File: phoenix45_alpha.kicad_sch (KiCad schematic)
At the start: 124 parts, among them J1 AVR-ISP-6, SW1 SW_PUSH, SW2 SW_PUSH, U1 SRV05-4, U3 ATmega32U4-M, X1 Crystal_GND24_Small

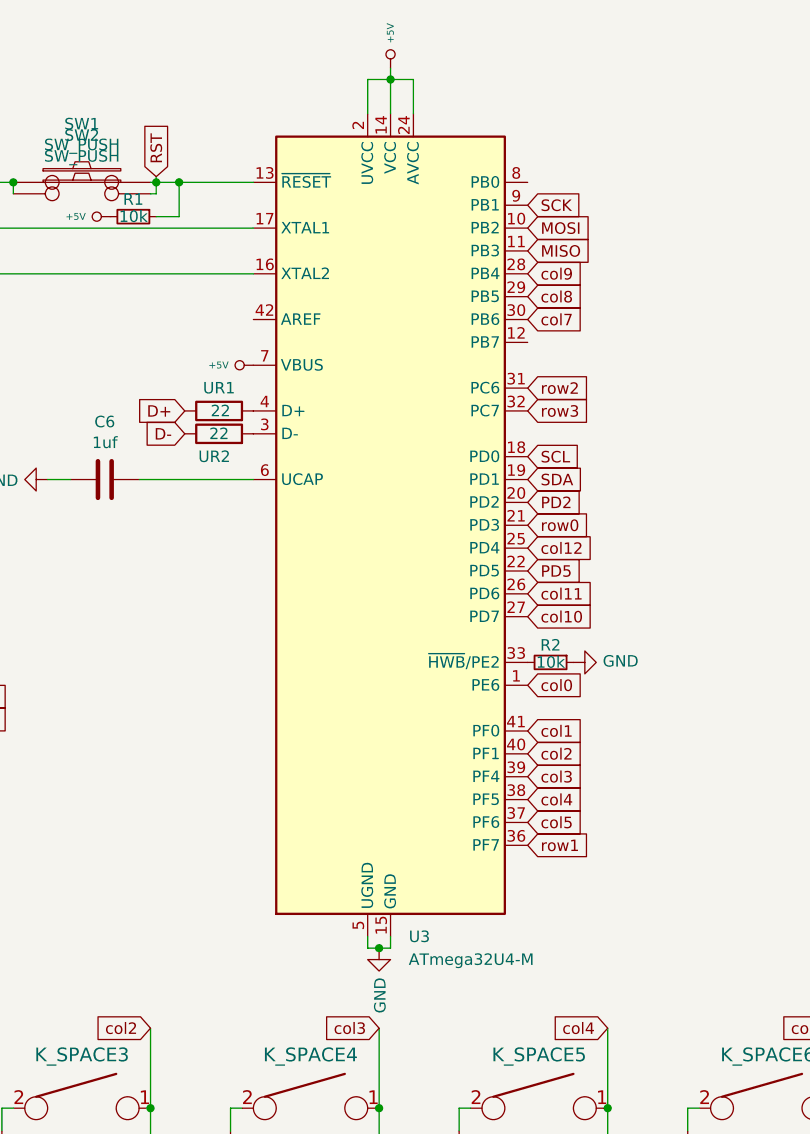
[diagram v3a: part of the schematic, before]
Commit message: qfn + tqfp
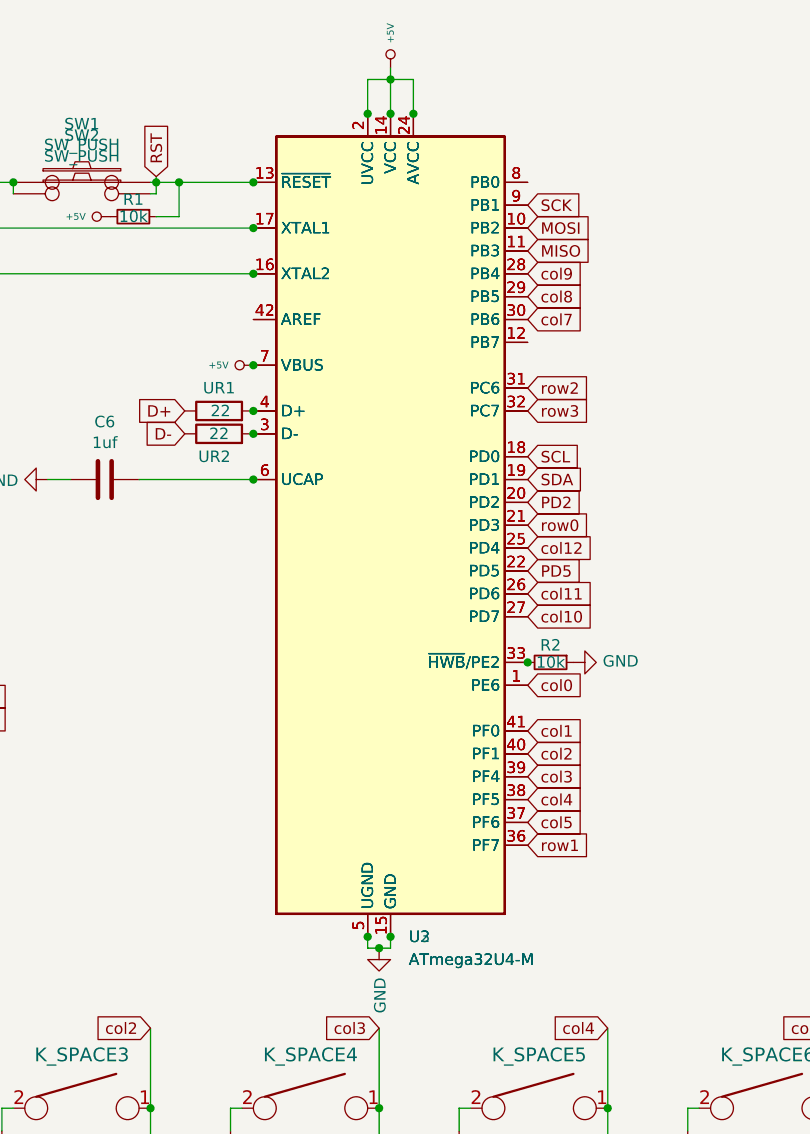
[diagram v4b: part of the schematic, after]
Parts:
- added U2: ATmega32U4-M, Package_DFN_QFN:QFN-44-1EP_7x7mm_P0.5mm_EP5.2x5.2mm_ThermalVias, symbol MCU_Microchip_ATmega:ATmega32U4-M
- U3: footprint Package_DFN_QFN:QFN-44-1EP_7x7mm_P0.5mm_EP5.2x5.2mm_ThermalVias -> Package_QFP:TQFP-44_10x10mm_P0.8mm
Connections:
- net +5V: now also U2.14 (VCC), U2.2 (UVCC), U2.24 (AVCC), U2.34 (VCC), U2.44 (AVCC), U2.7 (VBUS)
- net GND: now also U2.15 (GND), U2.23 (GND), U2.35 (GND), U2.43 (GND), U2.45 (GND), U2.5 (UGND)
- net MISO: now also U2.11 (PB3)
- net MOSI: now also U2.10 (PB2)
- net PD2: now also U2.20 (PD2)
- net PD5: now also U2.22 (PD5)
- net RST: now also U2.13 (~{RESET})
- net SCK: now also U2.9 (PB1)
- net SCL: now also U2.18 (PD0)
- net SDA: now also U2.19 (PD1)
- net col0: now also U2.1 (PE6)
- net col1: now also U2.41 (PF0)
- net col10: now also U2.27 (PD7)
- net col11: now also U2.26 (PD6)
- net col12: now also U2.25 (PD4)
- net col2: now also U2.40 (PF1)
- net col3: now also U2.39 (PF4)
- net col4: now also U2.38 (PF5)
- net col5: now also U2.37 (PF6)
- net col7: now also U2.30 (PB6)
- net col8: now also U2.29 (PB5)
- net col9: now also U2.28 (PB4)
- net row0: now also U2.21 (PD3)
- net row1: now also U2.36 (PF7)
- net row2: now also U2.31 (PC6)
- net row3: now also U2.32 (PC7)
- net at C7.1, U3.17 (XTAL1), X1.1: now also U2.17 (XTAL1)
- net at C8.1, U3.16 (XTAL2), X1.3: now also U2.16 (XTAL2)
- net at U3.4 (D+), UR2.2: now also U2.4 (D+)
- net at U3.3 (D-), UR1.2: now also U2.3 (D-)
- net at C6.1, U3.6 (UCAP): now also U2.6 (UCAP)
- net at R2.2, U3.33 (~{HWB}/PE2): now also U2.33 (~{HWB}/PE2)
- net at U3.12 (PB7): now also U2.12 (PB7)
- net at U3.42 (AREF): now also U2.42 (AREF)
- net at U3.8 (PB0): now also U2.8 (PB0)
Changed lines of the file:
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@@
   (junction (at 149.86 245.11) (diameter 0) (color 0 0 0 0)
   )
+  (junction (at 127 60.96) (diameter 0) (color 0 0 0 0)
+  )
   (junction (at 166.37 184.15) (diameter 0) (color 0 0 0 0)
   )
   (junction (at 233.045 66.675) (diameter 0) (color 0 0 0 0)
   )
+  (junction (at 142.24 48.26) (diameter 0) (color 0 0 0 0)
+  )
   (junction (at 140.97 158.75) (diameter 0) (color 0 0 0 0)
   )
@@
   (junction (at 140.97 140.97) (diameter 0) (color 0 0 0 0)
   )
+  (junction (at 139.7 139.7) (diameter 0) (color 0 0 0 0)
+  )
   (junction (at 251.46 219.71) (diameter 0) (color 0 0 0 0)
   )
   (junction (at 294.64 109.22) (diameter 0) (color 0 0 0 0)
   )
+  (junction (at 127 66.04) (diameter 0) (color 0 0 0 0)
+  )
   (junction (at 175.26 194.31) (diameter 0) (color 0 0 0 0)
   )
@@
   (junction (at 38.735 105.41) (diameter 0) (color 0 0 0 0)
   )
+  (junction (at 127 88.9) (diameter 0) (color 0 0 0 0)
+  )
   (junction (at 31.115 105.41) (diameter 0) (color 0 0 0 0)
   )
@@
   (junction (at 302.26 219.71) (diameter 0) (color 0 0 0 0)
   )
+  (junction (at 127 55.88) (diameter 0) (color 0 0 0 0)
+  )
   (junction (at 48.26 194.31) (diameter 0) (color 0 0 0 0)
   )
@@
   (junction (at 276.86 194.31) (diameter 0) (color 0 0 0 0)
   )
+  (junction (at 127 76.2) (diameter 0) (color 0 0 0 0)
+  )
   (junction (at 318.77 209.55) (diameter 0) (color 0 0 0 0)
   )
@@
   (junction (at 73.66 194.31) (diameter 0) (color 0 0 0 0)
   )
+  (junction (at 142.24 139.7) (diameter 0) (color 0 0 0 0)
+  )
   (junction (at 251.46 194.31) (diameter 0) (color 0 0 0 0)
   )
   (junction (at 318.77 158.75) (diameter 0) (color 0 0 0 0)
   )
+  (junction (at 139.7 48.26) (diameter 0) (color 0 0 0 0)
+  )
+  (junction (at 127 83.82) (diameter 0) (color 0 0 0 0)
+  )
   (junction (at 293.37 158.75) (diameter 0) (color 0 0 0 0)
   )
@@
   (junction (at 115.57 184.15) (diameter 0) (color 0 0 0 0)
   )
+  (junction (at 144.78 48.26) (diameter 0) (color 0 0 0 0)
+  )
   (junction (at 318.77 184.15) (diameter 0) (color 0 0 0 0)
   )
@@
   (junction (at 267.97 158.75) (diameter 0) (color 0 0 0 0)
   )
+  (junction (at 127 81.28) (diameter 0) (color 0 0 0 0)
+  )
   (junction (at 72.39 77.47) (diameter 0) (color 0 0 0 0)
   )
@@
   (junction (at 344.17 158.75) (diameter 0) (color 0 0 0 0)
   )
+  (junction (at 157.48 109.22) (diameter 0) (color 0 0 0 0)
+  )
   (junction (at 166.37 209.55) (diameter 0) (color 0 0 0 0)
   )
@@
     (pin "2")
   )
+  (symbol (lib_id "MCU_Microchip_ATmega:ATmega32U4-M") (at 142.24 93.98 0) (unit 1)
+    (in_bom yes) (on_board yes) (fields_autoplaced)
+    (property "Reference" "U2" (id 0) (at 144.2594 139.7 0)
+      (effects (font (size 1.27 1.27)) (justify left))
+    )
+    (property "Value" "ATmega32U4-M" (id 1) (at 144.2594 142.24 0)
+      (effects (font (size 1.27 1.27)) (justify left))
+    )
+    (property "Footprint" "Package_DFN_QFN:QFN-44-1EP_7x7mm_P0.5mm_EP5.2x5.2mm_ThermalVias" (id 2) (at 142.24 93.98 0)
+      (effects (font (size 1.27 1.27) italic) hide)
+    )
+    (property "Datasheet" "http://ww1.microchip.com/downloads/en/DeviceDoc/Atmel-7766-8-bit-AVR-ATmega16U4-32U4_Datasheet.pdf" (id 3) (at 142.24 93.98 0)
+      (effects (font (size 1.27 1.27)) hide)
+    )
+    (pin "1")
+    (pin "10")
+    (pin "11")
+    (pin "12")
+    (pin "13")
+    (pin "14")
+    (pin "15")
+    (pin "16")
+    (pin "17")
+    (pin "18")
+    (pin "19")
+    (pin "2")
+    (pin "20")
+    (pin "21")
+    (pin "22")
+    (pin "23")
+    (pin "24")
+    (pin "25")
+    (pin "26")
+    (pin "27")
+    (pin "28")
+    (pin "29")
+    (pin "3")
+    (pin "30")
+    (pin "31")
+    (pin "32")
+    (pin "33")
+    (pin "34")
+    (pin "35")
+    (pin "36")
+    (pin "37")
+    (pin "38")
+    (pin "39")
+    (pin "4")
+    (pin "40")
+    (pin "41")
+    (pin "42")
+    (pin "43")
+    (pin "44")
+    (pin "45")
+    (pin "5")
+    (pin "6")
+    (pin "7")
+    (pin "8")
+    (pin "9")
+  )
   (symbol (lib_id "keyboard_parts:SW_PUSH") (at 107.95 57.15 0) (unit 1)
     (in_bom yes) (on_board yes)
@@
   )
   (symbol (lib_id "MCU_Microchip_ATmega:ATmega32U4-M") (at 142.24 93.98 0) (unit 1)
-    (in_bom yes) (on_board yes) (fields_autoplaced)
+    (in_bom yes) (on_board yes)
     (property "Reference" "U3" (id 0) (at 144.2594 139.7 0)
       (effects (font (size 1.27 1.27)) (justify left))
@@
       (effects (font (size 1.27 1.27)) (justify left))
     )
-    (property "Footprint" "Package_DFN_QFN:QFN-44-1EP_7x7mm_P0.5mm_EP5.2x5.2mm_ThermalVias" (id 2) (at 142.24 93.98 0)
+    (property "Footprint" "Package_QFP:TQFP-44_10x10mm_P0.8mm" (id 2) (at 142.24 93.98 0)
       (effects (font (size 1.27 1.27) italic) hide)
     )
@@
       (reference "U1") (unit 1) (value "SRV05-4") (footprint "Package_TO_SOT_SMD:SOT-23-6_Handsoldering")
     )
+    (path "/1ced1425-3090-4db4-a173-4dd40d7cc299"
+      (reference "U2") (unit 1) (value "ATmega32U4-M") (footprint "Package_DFN_QFN:QFN-44-1EP_7x7mm_P0.5mm_EP5.2x5.2mm_ThermalVias")
+    )
     (path "/fe1a8f1c-b239-442d-acdc-13f4ebc5e42a"
-      (reference "U3") (unit 1) (value "ATmega32U4-M") (footprint "Package_DFN_QFN:QFN-44-1EP_7x7mm_P0.5mm_EP5.2x5.2mm_ThermalVias")
+      (reference "U3") (unit 1) (value "ATmega32U4-M") (footprint "Package_QFP:TQFP-44_10x10mm_P0.8mm")
     )
     (path "/5f7b6686-ca41-45e8-807e-4d2ae5a4c66e"

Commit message: THT
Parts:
- removed C9: 2.2uF, Capacitor_SMD:C_0805_2012Metric_Pad1.18x1.45mm_HandSolder, symbol device:C_Small
- added C9: 2.2uF, Capacitor_THT:CP_Radial_D4.0mm_P1.50mm, symbol Device:C_Polarized
- UR6, UR7, UR8: footprint Resistor_SMD:R_0805_2012Metric_Pad1.20x1.40mm_HandSolder -> Resistor_THT:R_Axial_DIN0207_L6.3mm_D2.5mm_P7.62mm_Horizontal
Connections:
- net +5V: now also C9.1
- net at TP5.1, UR8.1: now also C9.2
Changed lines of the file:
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@@
   (junction (at 175.26 168.91) (diameter 0) (color 0 0 0 0)
   )
+  (junction (at 276.86 116.84) (diameter 0) (color 0 0 0 0)
+  )
   (junction (at 166.37 158.75) (diameter 0) (color 0 0 0 0)
   )
@@
   (junction (at 369.57 204.47) (diameter 0) (color 0 0 0 0)
   )
-  (junction (at 276.86 116.84) (diameter 0) (color 0 0 0 0)
-  )
   (junction (at 344.17 209.55) (diameter 0) (color 0 0 0 0)
   )
@@
     (stroke (width 0) (type default) (color 0 0 0 0))
   )
-  (wire (pts (xy 276.86 116.84) (xy 285.75 116.84))
+  (wire (pts (xy 260.35 116.84) (xy 276.86 116.84))
     (stroke (width 0) (type default) (color 0 0 0 0))
   )
@@
     (stroke (width 0) (type default) (color 0 0 0 0))
   )
+  (wire (pts (xy 276.86 116.84) (xy 276.86 128.27))
+    (stroke (width 0) (type default) (color 0 0 0 0))
+  )
   (wire (pts (xy 176.53 158.75) (xy 175.26 158.75))
     (stroke (width 0) (type default) (color 0 0 0 0))
@@
     (stroke (width 0) (type default) (color 0 0 0 0))
   )
-  (wire (pts (xy 260.35 116.84) (xy 276.86 116.84))
-    (stroke (width 0) (type default) (color 0 0 0 0))
-  )
   (wire (pts (xy 226.06 158.75) (xy 226.06 161.29))
     (stroke (width 0) (type default) (color 0 0 0 0))
@@
     (stroke (width 0) (type default) (color 0 0 0 0))
   )
-  (wire (pts (xy 276.86 116.84) (xy 276.86 130.81))
-    (stroke (width 0) (type default) (color 0 0 0 0))
-  )
   (wire (pts (xy 226.06 234.95) (xy 226.06 237.49))
     (stroke (width 0) (type default) (color 0 0 0 0))
@@
     (stroke (width 0) (type default) (color 0 0 0 0))
   )
+  (wire (pts (xy 276.86 116.84) (xy 285.75 116.84))
+    (stroke (width 0) (type default) (color 0 0 0 0))
+  )
   (wire (pts (xy 124.46 194.31) (xy 149.86 194.31))
     (stroke (width 0) (type default) (color 0 0 0 0))
@@
     (property "Reference" "UR8" (id 0) (at 268.605 132.08 90))
     (property "Value" "100k" (id 1) (at 270.51 132.08 90))
-    (property "Footprint" "Resistor_SMD:R_0805_2012Metric_Pad1.20x1.40mm_HandSolder" (id 2) (at 272.288 132.08 90)
+    (property "Footprint" "Resistor_THT:R_Axial_DIN0207_L6.3mm_D2.5mm_P7.62mm_Horizontal" (id 2) (at 272.288 132.08 90)
       (effects (font (size 1.27 1.27)) hide)
     )
@@
     (pin "2")
   )
+  (symbol (lib_id "Device:C_Polarized") (at 276.86 132.08 0) (unit 1)
+    (in_bom yes) (on_board yes) (fields_autoplaced)
+    (property "Reference" "C9" (id 0) (at 280.67 129.9209 0)
+      (effects (font (size 1.27 1.27)) (justify left))
+    )
+    (property "Value" "2.2uF" (id 1) (at 280.67 132.4609 0)
+      (effects (font (size 1.27 1.27)) (justify left))
+    )
+    (property "Footprint" "Capacitor_THT:CP_Radial_D4.0mm_P1.50mm" (id 2) (at 277.8252 135.89 0)
+      (effects (font (size 1.27 1.27)) hide)
+    )
+    (property "Datasheet" "~" (id 3) (at 276.86 132.08 0)
+      (effects (font (size 1.27 1.27)) hide)
+    )
+    (pin "1")
+    (pin "2")
+  )
   (symbol (lib_id "Power_Protection:SRV05-4") (at 270.51 73.66 270) (unit 1)
     (in_bom yes) (on_board yes) (fields_autoplaced)
@@
     (pin "2")
   )
-  (symbol (lib_id "device:C_Small") (at 276.86 133.35 0) (unit 1)
-    (in_bom yes) (on_board yes)
-    (property "Reference" "C9" (id 0) (at 279.4 133.35 90))
-    (property "Value" "2.2uF" (id 1) (at 281.305 133.35 90))
-    (property "Footprint" "Capacitor_SMD:C_0805_2012Metric_Pad1.18x1.45mm_HandSolder" (id 2) (at 276.86 133.35 0)
-      (effects (font (size 1.27 1.27)) hide)
-    )
-    (property "Datasheet" "~" (id 3) (at 276.86 133.35 0)
-      (effects (font (size 1.27 1.27)) hide)
-    )
-    (pin "1")
-    (pin "2")
-  )
   (symbol (lib_id "keyboard_parts:KEYSW") (at 285.75 158.75 0) (unit 1)
     (in_bom yes) (on_board yes)
@@
     (property "Reference" "UR7" (id 0) (at 283.845 125.73 90))
     (property "Value" "4.7k" (id 1) (at 285.75 125.73 90))
-    (property "Footprint" "Resistor_SMD:R_0805_2012Metric_Pad1.20x1.40mm_HandSolder" (id 2) (at 287.528 125.73 90)
+    (property "Footprint" "Resistor_THT:R_Axial_DIN0207_L6.3mm_D2.5mm_P7.62mm_Horizontal" (id 2) (at 287.528 125.73 90)
       (effects (font (size 1.27 1.27)) hide)
     )
@@
     (property "Reference" "UR6" (id 0) (at 292.735 113.03 90))
     (property "Value" "4.7k" (id 1) (at 294.64 113.03 90))
-    (property "Footprint" "Resistor_SMD:R_0805_2012Metric_Pad1.20x1.40mm_HandSolder" (id 2) (at 296.418 113.03 90)
+    (property "Footprint" "Resistor_THT:R_Axial_DIN0207_L6.3mm_D2.5mm_P7.62mm_Horizontal" (id 2) (at 296.418 113.03 90)
       (effects (font (size 1.27 1.27)) hide)
     )
@@
       (reference "C8") (unit 1) (value "22p") (footprint "Capacitor_SMD:C_0805_2012Metric_Pad1.18x1.45mm_HandSolder")
     )
-    (path "/80008935-f437-4413-9bb4-4410c098a61c"
-      (reference "C9") (unit 1) (value "2.2uF") (footprint "Capacitor_SMD:C_0805_2012Metric_Pad1.18x1.45mm_HandSolder")
+    (path "/4025392c-7a2d-453f-ac00-29ea71e6d61c"
+      (reference "C9") (unit 1) (value "2.2uF") (footprint "Capacitor_THT:CP_Radial_D4.0mm_P1.50mm")
     )
     (path "/b1cf07dc-bdc6-4ab5-ac0e-8b5804ad86ba"
@@
     )
     (path "/e0224c52-a5ee-4555-b923-3d2a879c54dd"
-      (reference "UR6") (unit 1) (value "4.7k") (footprint "Resistor_SMD:R_0805_2012Metric_Pad1.20x1.40mm_HandSolder")
+      (reference "UR6") (unit 1) (value "4.7k") (footprint "Resistor_THT:R_Axial_DIN0207_L6.3mm_D2.5mm_P7.62mm_Horizontal")
     )
     (path "/8d00e43a-de53-4705-b6e9-0a3e4ea35179"
-      (reference "UR7") (unit 1) (value "4.7k") (footprint "Resistor_SMD:R_0805_2012Metric_Pad1.20x1.40mm_HandSolder")
+      (reference "UR7") (unit 1) (value "4.7k") (footprint "Resistor_THT:R_Axial_DIN0207_L6.3mm_D2.5mm_P7.62mm_Horizontal")
     )
     (path "/181c24dd-5019-490d-b286-99fa857df313"
-      (reference "UR8") (unit 1) (value "100k") (footprint "Resistor_SMD:R_0805_2012Metric_Pad1.20x1.40mm_HandSolder")
+      (reference "UR8") (unit 1) (value "100k") (footprint "Resistor_THT:R_Axial_DIN0207_L6.3mm_D2.5mm_P7.62mm_Horizontal")
     )
     (path "/b93d027f-21f6-4fc9-ad3f-317eded6973b"
